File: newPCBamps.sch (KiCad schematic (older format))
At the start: 7 parts

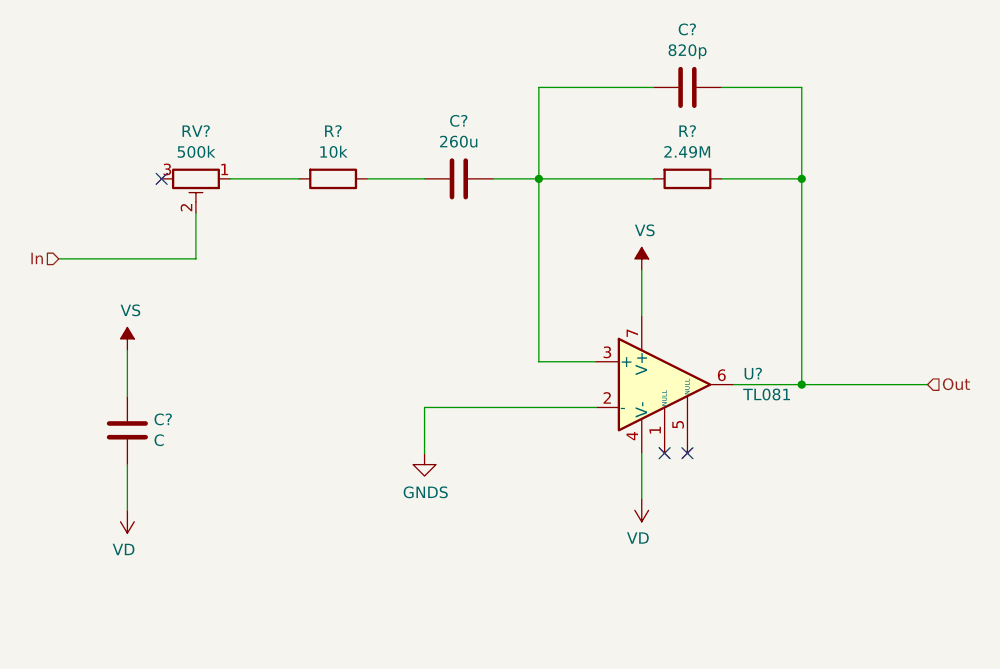
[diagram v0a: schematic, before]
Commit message: Added bypass capacitors to newPCBamps layer, need to implement analog ground in top layer
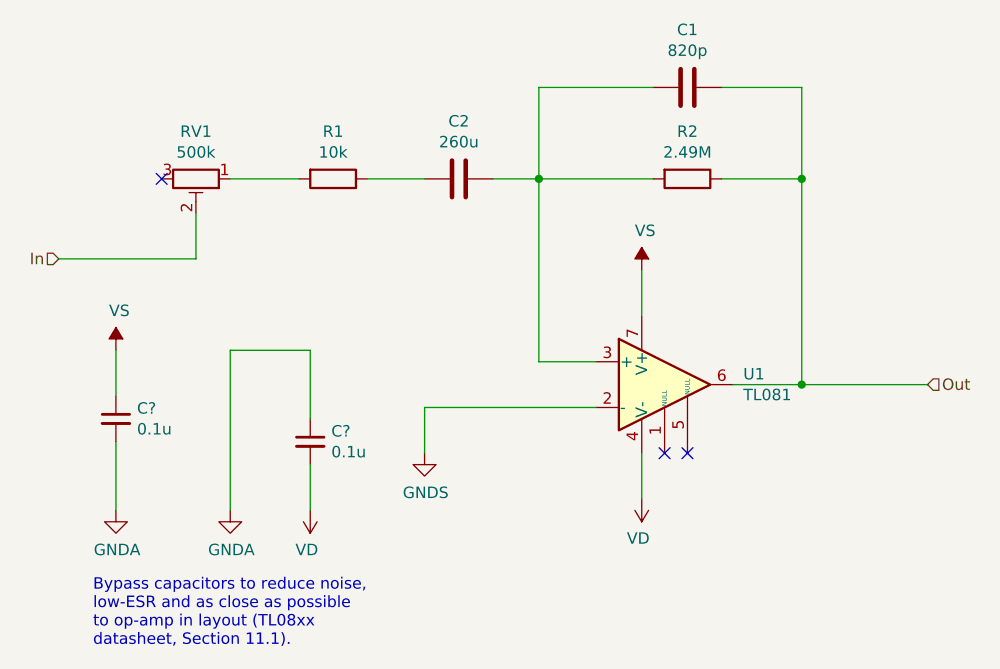
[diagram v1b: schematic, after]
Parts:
- removed C?: C, symbol Device:C
- added C? (x2): 0.1u, symbol Device:C_Small
- gave numbers to parts that had none: 6
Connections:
- net VD: now also C?.2
- net VS: now also C?.1
- new net GNDA: C?.1, C?.2
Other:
- note added: "Bypass capacitors to reduce noise, \nlow-ESR and as close as possible \nto op-amp in layout (TL08xx \ndatasheet, Section 11.1)."
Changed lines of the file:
@@
 	5300 4300 6050 4300
 $Comp
-L power:GNDS #PWR?
+L power:GNDS #PWR03
 U 1 1 6227322D
 P 5300 4500
-F 0 "#PWR?" H 5300 4250 50  0001 C CNN
+F 0 "#PWR03" H 5300 4250 50  0001 C CNN
 F 1 "GNDS" H 5305 4327 50  0000 C CNN
 F 2 "" H 5300 4500 50  0001 C CNN
@@
 	6950 2900 6950 3300
 $Comp
-L Device:C C?
+L Device:C C1
 U 1 1 62273235
 P 6450 2900
-F 0 "C?" V 6198 2900 50  0000 C CNN
+F 0 "C1" V 6198 2900 50  0000 C CNN
 F 1 "820p" V 6289 2900 50  0000 C CNN
 F 2 "Capacitor_SMD:C_1210_3225Metric_Pad1.42x2.65mm_HandSolder" H 6488 2750 50  0001 C CNN
@@
 $EndComp
 $Comp
-L Device:R R?
+L Device:R R2
 U 1 1 6227323B
 P 6450 3300
-F 0 "R?" V 6243 3300 50  0000 C CNN
+F 0 "R2" V 6243 3300 50  0000 C CNN
 F 1 "2.49M" V 6334 3300 50  0000 C CNN
 F 2 "Resistor_SMD:R_0612_1632Metric_Pad1.18x3.40mm_HandSolder" V 6380 3300 50  0001 C CNN
@@
 	4300 3450 4300 3650
 $Comp
-L Device:R_POT_TRIM RV?
+L Device:R_POT_TRIM RV1
 U 1 1 62273243
 P 4300 3300
-F 0 "RV?" V 4093 3300 50  0000 C CNN
+F 0 "RV1" V 4093 3300 50  0000 C CNN
 F 1 "500k" V 4184 3300 50  0000 C CNN
 F 2 "Potentiometer_THT:Potentiometer_Vishay_148-149_Single_Vertical" H 4300 3300 50  0001 C CNN
@@
 $EndComp
 $Comp
-L Device:R R?
+L Device:R R1
 U 1 1 62273249
 P 4900 3300
-F 0 "R?" V 4693 3300 50  0000 C CNN
+F 0 "R1" V 4693 3300 50  0000 C CNN
 F 1 "10k" V 4784 3300 50  0000 C CNN
 F 2 "Resistor_SMD:R_0612_1632Metric_Pad1.18x3.40mm_HandSolder" V 4830 3300 50  0001 C CNN
@@
 $EndComp
 $Comp
-L Device:C C?
+L Device:C C2
 U 1 1 6227324F
 P 5450 3300
-F 0 "C?" V 5198 3300 50  0000 C CNN
+F 0 "C2" V 5198 3300 50  0000 C CNN
 F 1 "260u" V 5289 3300 50  0000 C CNN
 F 2 "Capacitor_THT:CP_Radial_D40.0mm_P10.00mm_3pin_SnapIn" H 5488 3150 50  0001 C CNN
@@
 NoConn ~ 6450 4500
 $Comp
-L Amplifier_Operational:TL081 U?
+L Amplifier_Operational:TL081 U1
 U 1 1 6227325A
 P 6350 4200
-F 0 "U?" H 6694 4246 50  0000 L CNN
+F 0 "U1" H 6694 4246 50  0000 L CNN
 F 1 "TL081" H 6694 4155 50  0000 L CNN
 F 2 "" H 6400 4250 50  0001 C CNN
@@
 Connection ~ 6950 4200
 $Comp
-L power:VD #PWR?
+L power:VD #PWR04
 U 1 1 62273268
 P 6250 4700
-F 0 "#PWR?" H 6250 4550 50  0001 C CNN
+F 0 "#PWR04" H 6250 4550 50  0001 C CNN
 F 1 "VD" H 6265 4873 50  0000 C CNN
 F 2 "" H 6250 4700 50  0001 C CNN
@@
 $EndComp
 $Comp
-L power:VS #PWR?
+L power:VS #PWR01
 U 1 1 6227326E
 P 6250 3700
-F 0 "#PWR?" H 6050 3550 50  0001 C CNN
+F 0 "#PWR01" H 6050 3550 50  0001 C CNN
 F 1 "VS" H 6265 3873 50  0000 C CNN
 F 2 "" H 6250 3700 50  0001 C CNN
@@
 	6950 4200 7500 4200
 $Comp
-L power:VS #PWR?
+L power:VS #PWR02
 U 1 1 62273276
-P 4000 4050
-F 0 "#PWR?" H 3800 3900 50  0001 C CNN
-F 1 "VS" H 4015 4223 50  0000 C CNN
-F 2 "" H 4000 4050 50  0001 C CNN
-F 3 "" H 4000 4050 50  0001 C CNN
-	1    4000 4050
-	1    0    0    -1
-$EndComp
-$Comp
-L power:VD #PWR?
+P 3950 4050
+F 0 "#PWR02" H 3750 3900 50  0001 C CNN
+F 1 "VS" H 3965 4223 50  0000 C CNN
+F 2 "" H 3950 4050 50  0001 C CNN
+F 3 "" H 3950 4050 50  0001 C CNN
+	1    3950 4050
+	1    0    0    -1
+$EndComp
+$Comp
+L power:VD #PWR05
 U 1 1 6227327C
-P 4000 4750
-F 0 "#PWR?" H 4000 4600 50  0001 C CNN
-F 1 "VD" H 4015 4923 50  0000 C CNN
-F 2 "" H 4000 4750 50  0001 C CNN
-F 3 "" H 4000 4750 50  0001 C CNN
-	1    4000 4750
+P 4800 4750
+F 0 "#PWR05" H 4800 4600 50  0001 C CNN
+F 1 "VD" H 4815 4923 50  0000 C CNN
+F 2 "" H 4800 4750 50  0001 C CNN
+F 3 "" H 4800 4750 50  0001 C CNN
+	1    4800 4750
 	-1   0    0    1
 $EndComp
-$Comp
-L Device:C C?
-U 1 1 62273282
-P 4000 4400
-F 0 "C?" H 4115 4446 50  0000 L CNN
-F 1 "C" H 4115 4355 50  0000 L CNN
-F 2 "" H 4038 4250 50  0001 C CNN
-F 3 "~" H 4000 4400 50  0001 C CNN
-	1    4000 4400
-	1    0    0    -1
-$EndComp
-Wire Wire Line
-	4000 4550 4000 4750
-Wire Wire Line
-	4000 4250 4000 4050
+Wire Wire Line
+	4800 4550 4800 4750
+Wire Wire Line
+	3950 4250 3950 4050
 Text HLabel 3700 3650 0    50   Input ~ 0
 In
 Text HLabel 7500 4200 2    50   Input ~ 0
 Out
+$Comp
+L Device:C_Small C?
+U 1 1 62258B8A
+P 3950 4350
+F 0 "C?" H 4042 4396 50  0000 L CNN
+F 1 "0.1u" H 4042 4305 50  0000 L CNN
+F 2 "" H 3950 4350 50  0001 C CNN
+F 3 "~" H 3950 4350 50  0001 C CNN
+	1    3950 4350
+	1    0    0    -1
+$EndComp
+$Comp
+L Device:C_Small C?
+U 1 1 6225941E
+P 4800 4450
+F 0 "C?" H 4892 4496 50  0000 L CNN
+F 1 "0.1u" H 4892 4405 50  0000 L CNN
+F 2 "" H 4800 4450 50  0001 C CNN
+F 3 "~" H 4800 4450 50  0001 C CNN
+	1    4800 4450
+	1    0    0    -1
+$EndComp
+$Comp
+L power:GNDA #PWR?
+U 1 1 6225BF76
+P 3950 4750
+F 0 "#PWR?" H 3950 4500 50  0001 C CNN
+F 1 "GNDA" H 3955 4577 50  0000 C CNN
+F 2 "" H 3950 4750 50  0001 C CNN
+F 3 "" H 3950 4750 50  0001 C CNN
+	1    3950 4750
+	1    0    0    -1
+$EndComp
+$Comp
+L power:GNDA #PWR?
+U 1 1 6225C8A2
+P 4450 4750
+F 0 "#PWR?" H 4450 4500 50  0001 C CNN
+F 1 "GNDA" H 4455 4577 50  0000 C CNN
+F 2 "" H 4450 4750 50  0001 C CNN
+F 3 "" H 4450 4750 50  0001 C CNN
+	1    4450 4750
+	1    0    0    -1
+$EndComp
+Wire Wire Line
+	4800 4050 4800 4350
+Wire Wire Line
+	4800 4050 4450 4050
+Wire Wire Line
+	4450 4050 4450 4750
+Wire Wire Line
+	3950 4750 3950 4450
+Text Notes 3850 5350 0    50   ~ 0
+Bypass capacitors to reduce noise, \nlow-ESR and as close as possible \nto op-amp in layout (TL08xx \ndatasheet, Section 11.1).
 $EndSCHEMATC
